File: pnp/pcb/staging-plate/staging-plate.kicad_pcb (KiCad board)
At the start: 2 copper layers, 600 x 120 mm, 140 parts

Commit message: Fix graphics attributes
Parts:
- renumbered G*** to G3
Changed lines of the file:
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@@
 		(layer "B.Cu")
 		(at 138.6 108.4)
-		(property "Reference" "G***"
+		(property "Reference" "G3"
 			(at 0 0 0)
 			(layer "B.SilkS")
@@
 			)
 		)
-		(attr through_hole)
+		(attr through_hole board_only exclude_from_pos_files exclude_from_bom)
 		(fp_poly
 			(pts

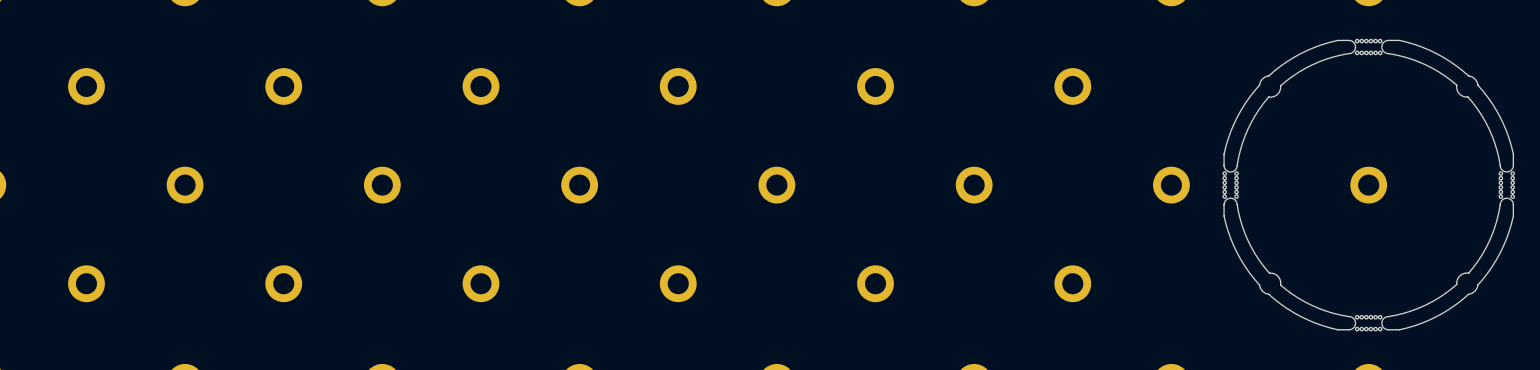
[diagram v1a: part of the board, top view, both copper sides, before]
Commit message: adds new offset camera cutout to staging plate at column 8
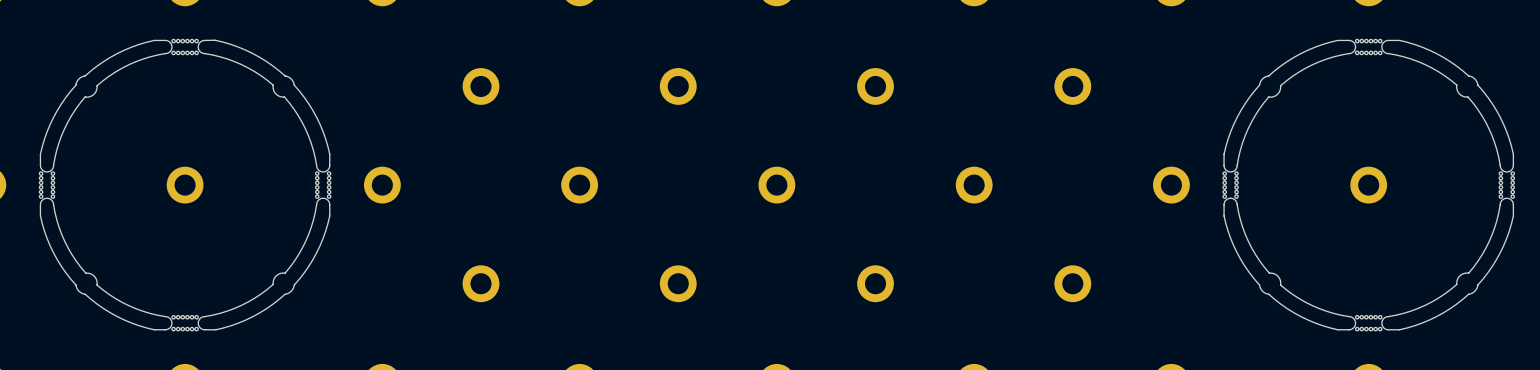
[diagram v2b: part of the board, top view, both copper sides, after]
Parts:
- removed the ? at (-56.0, 81.0)
- removed the ? at (-26.0, 81.0)
- removed the ? at (-26.0, 111.0)
- removed the ? at (-56.0, 111.0)
- added G3: LOGO, mfg:goblin-tiny, B.Cu at (-41.4, 108.4)
- added mouse-bite-2mm-slot: VAL**, Panelization:mouse-bite-2mm-slot-4mm, F.Cu at (-62.0, 96.0)
- added mouse-bite-2mm-slot: VAL**, Panelization:mouse-bite-2mm-slot-4mm, F.Cu at (-20.0, 96.0)
- added mouse-bite-2mm-slot: VAL**, Panelization:mouse-bite-2mm-slot-4mm, F.Cu at (-41.0, 117.0)
- added mouse-bite-2mm-slot: VAL**, Panelization:mouse-bite-2mm-slot-4mm, F.Cu at (-41.0, 75.0)
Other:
- outline, holes or cut-outs redrawn

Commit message: exported rev01b0 of staging plate
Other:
- board text added: "LumenPnP Staging Plate REV01"
- board text removed: "LumenPnP Staging Plate REV00"
